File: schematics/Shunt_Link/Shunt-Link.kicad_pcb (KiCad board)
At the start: 2 copper layers, 78.2 x 96 mm, 33 parts, among them IC1 AD8221TRMZ-EP, IC2 AD8221TRMZ-EP, IC3 AD8221TRMZ-EP, IC4 AD8221TRMZ-EP, J1 PCIE-036-02-X-D-TH, J2 Conn_02x03_Odd_Even, J3 Conn_02x03_Odd_Even

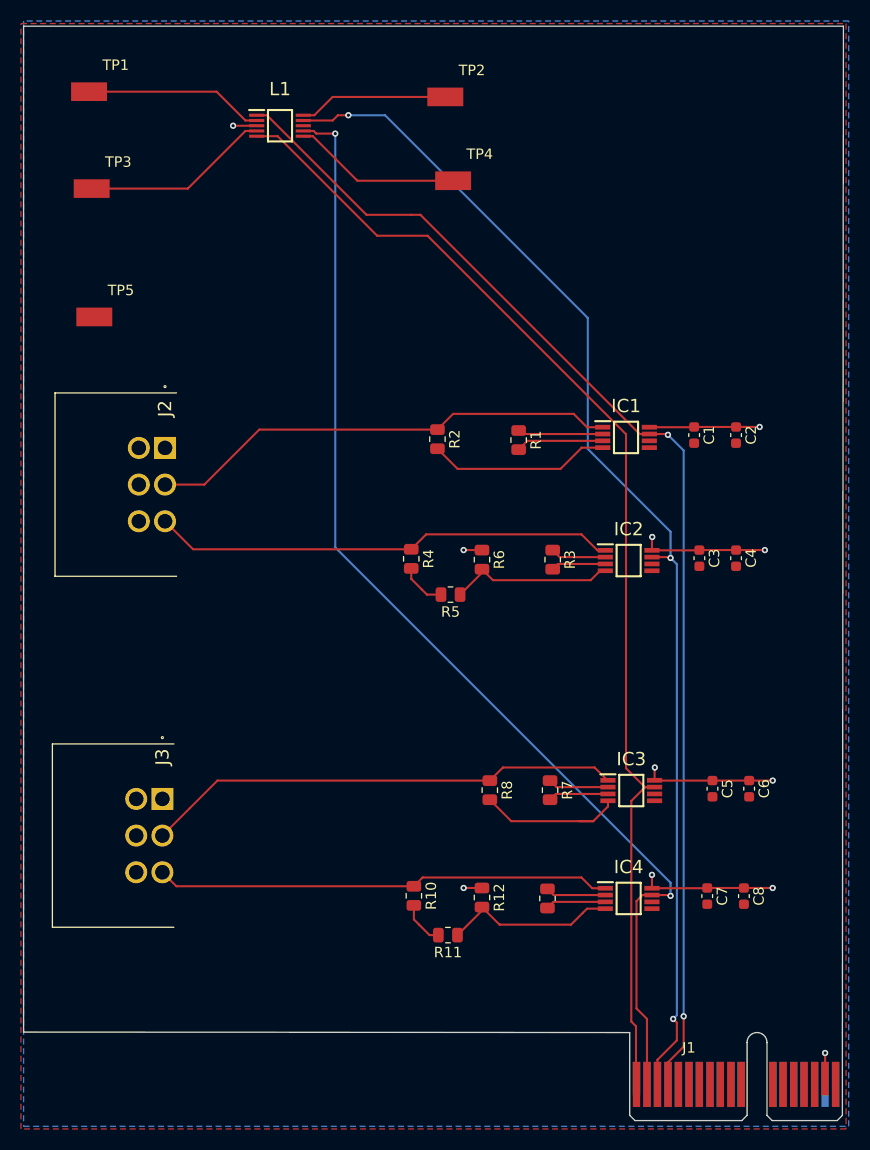
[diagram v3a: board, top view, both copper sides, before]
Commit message: Update libraries to one lib for all projects
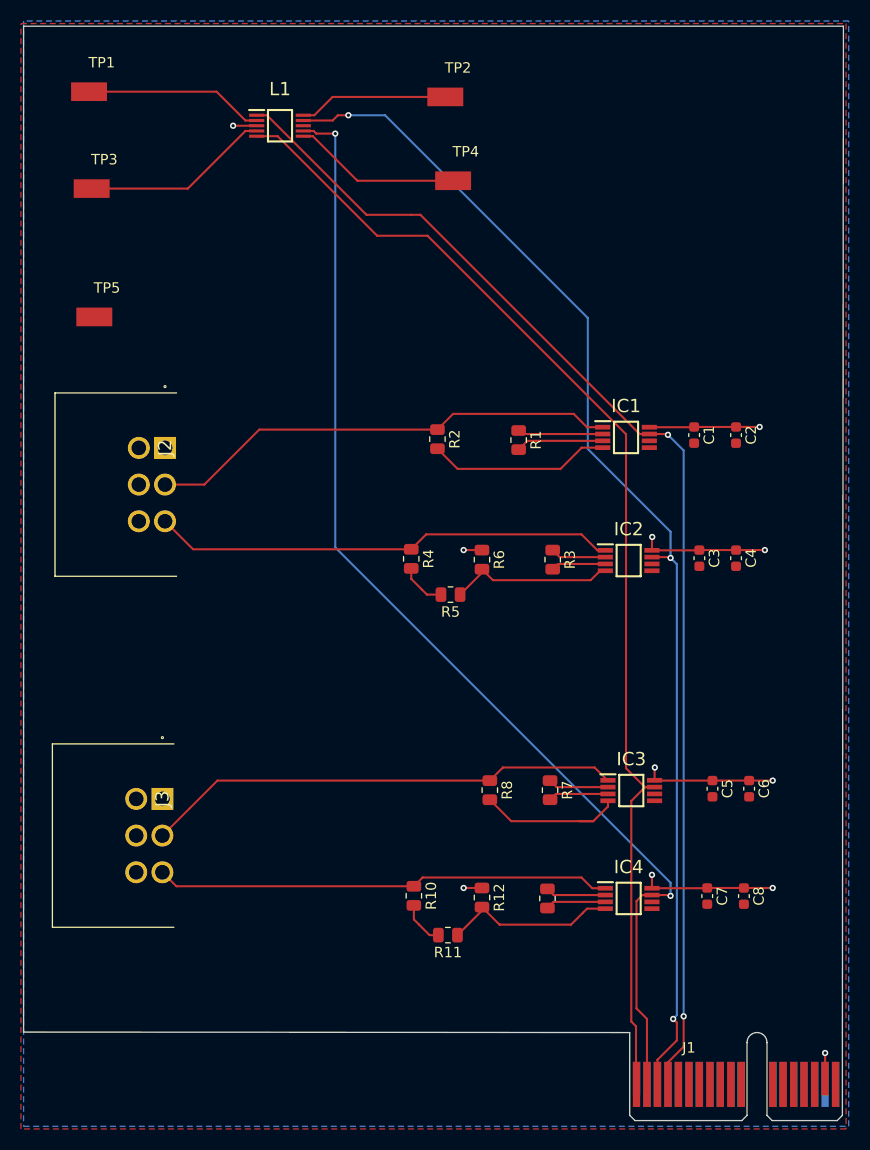
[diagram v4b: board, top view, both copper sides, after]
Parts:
- IC1, IC2, IC3, IC4: footprint Link_Footprints:AD8221TRMZ-EP -> Link Footprints:AD8221TRMZ
- J2, J3: footprint Link_Footprints:1818517 -> Link Footprints:PC-1818517
- L1: footprint Link_Footprints:AD8244ARMZ -> Link Footprints:AD8244ARMZ
- TP1, TP2, TP3, TP4, TP5: footprint Link_Footprints:KEYSTONE_5017 -> Link Footprints:Keystone_5017
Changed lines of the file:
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@@
 		)
 	)
-	(footprint "Link_Footprints:AD8221TRMZ-EP"
+	(footprint "Link Footprints:AD8221TRMZ"
 		(layer "F.Cu")
 		(at 135 66)
@@
 			)
 		)
+		(property "Field4" ""
+			(at 0 0 0)
+			(layer "F.SilkS")
+			(effects
+				(font
+					(size 1 1)
+					(thickness 0.1)
+				)
+			)
+		)
 		(property "Height" "1.1"
 			(at 0 0 0)
@@
 		)
 		(embedded_fonts no)
-		(model "C:/Users/smbea/OneDrive/Personal Files/School/Summer 2025/KiCad Lib Files/AD8221TRMZ/AD8221.step"
+		(model "${KIPRJMOD}/../libraries/models/AD8221TRMZ.step"
 			(offset
 				(xyz 0 0 0)
@@
 		(embedded_fonts no)
 	)
-	(footprint "Link_Footprints:KEYSTONE_5017"
+	(footprint "Link Footprints:Keystone_5017"
 		(layer "F.Cu")
 		(at 117.75 33.5)
 		(property "Reference" "TP2"
-			(at 2.54 -2.54 0)
+			(at 1.21 -2.775 0)
 			(layer "F.SilkS")
 			(effects
@@
 		)
 		(property "Value" "T1"
-			(at -2.54 -2.54 0)
+			(at 6.29 2.775 0)
 			(layer "F.Fab")
 			(effects
@@
 			(layer "F.Fab")
 		)
-		(pad "1" smd rect
+		(pad "TP" smd rect
 			(at 0 0)
 			(size 3.43 1.78)
 			(layers "F.Cu" "F.Mask" "F.Paste")
-			(net 52 "/T_{1test}")
-			(pinfunction "1")
-			(pintype "passive")
 			(solder_mask_margin 0.102)
 		)
 		(embedded_fonts no)
-		(model "C:/Users/smbea/OneDrive/Personal_Files/School/Fall_2025/OATS/avena-rs/schematics/KiCad Lib Files/Keystone_5017/5017.STEP"
+		(model "${KIPRJMOD}/../libraries/models/Keystone_5017.STEP"
 			(offset
 				(xyz 0 0 0)
@@
 		)
 	)
-	(footprint "Link_Footprints:AD8244ARMZ"
+	(footprint "Link Footprints:AD8244ARMZ"
 		(layer "F.Cu")
 		(at 101.975 36.25)
@@
 		)
 		(embedded_fonts no)
-		(model "C:/Users/smbea/OneDrive/Personal Files/School/Summer 2025/KiCad Lib Files/AD8244/AD8244ARMZ.stp"
+		(model "${KIPRJMOD}/../libraries/models/AD8244ARMZ.stp"
 			(offset
 				(xyz 0 0 0)
@@
 		)
 	)
-	(footprint "Link_Footprints:AD8221TRMZ-EP"
+	(footprint "Link Footprints:AD8221TRMZ"
 		(layer "F.Cu")
 		(at 135.5 99.7)
@@
 			)
 		)
+		(property "Field4" ""
+			(at 0 0 0)
+			(layer "F.SilkS")
+			(effects
+				(font
+					(size 1 1)
+					(thickness 0.1)
+				)
+			)
+		)
 		(property "Height" "1.1"
 			(at 0 0 0)
@@
 		)
 		(embedded_fonts no)
-		(model "C:/Users/smbea/OneDrive/Personal Files/School/Summer 2025/KiCad Lib Files/AD8221TRMZ/AD8221.step"
+		(model "${KIPRJMOD}/../libraries/models/AD8221TRMZ.step"
 			(offset
 				(xyz 0 0 0)
@@
 		)
 	)
-	(footprint "Link_Footprints:KEYSTONE_5017"
+	(footprint "Link Footprints:Keystone_5017"
 		(layer "F.Cu")
 		(at 83.75 33)
 		(property "Reference" "TP1"
-			(at 2.54 -2.54 0)
+			(at 1.21 -2.775 0)
 			(layer "F.SilkS")
 			(effects
@@
 		)
 		(property "Value" "S1"
-			(at -2.54 -2.54 0)
+			(at 6.29 2.775 0)
 			(layer "F.Fab")
 			(effects
@@
 			(layer "F.Fab")
 		)
-		(pad "1" smd rect
+		(pad "TP" smd rect
 			(at 0 0)
 			(size 3.43 1.78)
 			(layers "F.Cu" "F.Mask" "F.Paste")
-			(net 51 "/S_{1test}")
-			(pinfunction "1")
-			(pintype "passive")
 			(solder_mask_margin 0.102)
 		)
 		(embedded_fonts no)
-		(model "C:/Users/smbea/OneDrive/Personal_Files/School/Fall_2025/OATS/avena-rs/schematics/KiCad Lib Files/Keystone_5017/5017.STEP"
+		(model "${KIPRJMOD}/../libraries/models/Keystone_5017.STEP"
 			(offset
 				(xyz 0 0 0)
@@
 		)
 	)
-	(footprint "Link_Footprints:AD8221TRMZ-EP"
+	(footprint "Link Footprints:AD8221TRMZ"
 		(layer "F.Cu")
 		(at 135.25 77.75)
@@
 			)
 		)
+		(property "Field4" ""
+			(at 0 0 0)
+			(layer "F.SilkS")
+			(effects
+				(font
+					(size 1 1)
+					(thickness 0.1)
+				)
+			)
+		)
 		(property "Height" "1.1"
 			(at 0 0 0)
@@
 		)
 		(embedded_fonts no)
-		(model "C:/Users/smbea/OneDrive/Personal Files/School/Summer 2025/KiCad Lib Files/AD8221TRMZ/AD8221.step"
+		(model "${KIPRJMOD}/../libraries/models/AD8221TRMZ.step"
 			(offset
 				(xyz 0 0 0)
@@
 		)
 	)
-	(footprint "Link_Footprints:KEYSTONE_5017"
+	(footprint "Link Footprints:Keystone_5017"
 		(layer "F.Cu")
 		(at 84 42.25)
 		(property "Reference" "TP3"
-			(at 2.54 -2.54 0)
+			(at 1.21 -2.775 0)
 			(layer "F.SilkS")
 			(effects
@@
 		)
 		(property "Value" "S2"
-			(at -2.54 -2.54 0)
+			(at 6.29 2.775 0)
 			(layer "F.Fab")
 			(effects
@@
 			(layer "F.Fab")
 		)
-		(pad "1" smd rect
+		(pad "TP" smd rect
 			(at 0 0)
 			(size 3.43 1.78)
 			(layers "F.Cu" "F.Mask" "F.Paste")
-			(net 53 "/S_{2test}")
-			(pinfunction "1")
-			(pintype "passive")
 			(solder_mask_margin 0.102)
 		)
 		(embedded_fonts no)
-		(model "C:/Users/smbea/OneDrive/Personal_Files/School/Fall_2025/OATS/avena-rs/schematics/KiCad Lib Files/Keystone_5017/5017.STEP"
+		(model "${KIPRJMOD}/../libraries/models/Keystone_5017.STEP"
 			(offset
 				(xyz 0 0 0)
@@
 		)
 	)
-	(footprint "Link_Footprints:KEYSTONE_5017"
+	(footprint "Link Footprints:Keystone_5017"
 		(layer "F.Cu")
 		(at 84.25 54.5)
 		(property "Reference" "TP5"
-			(at 2.54 -2.54 0)
+			(at 1.21 -2.775 0)
 			(layer "F.SilkS")
 			(effects
@@
 		)
 		(property "Value" "GND"
-			(at -2.54 -2.54 0)
+			(at 6.29 2.775 0)
 			(layer "F.Fab")
 			(effects
@@
 			(layer "F.Fab")
 		)
-		(pad "1" smd rect
+		(pad "TP" smd rect
 			(at 0 0)
 			(size 3.43 1.78)
 			(layers "F.Cu" "F.Mask" "F.Paste")
-			(net 1 "GND")
-			(pinfunction "1")
-			(pintype "passive")
 			(solder_mask_margin 0.102)
 		)
 		(embedded_fonts no)
-		(model "C:/Users/smbea/OneDrive/Personal_Files/School/Fall_2025/OATS/avena-rs/schematics/KiCad Lib Files/Keystone_5017/5017.STEP"
+		(model "${KIPRJMOD}/../libraries/models/Keystone_5017.STEP"
 			(offset
 				(xyz 0 0 0)
@@
 		)
 	)
-	(footprint "Link_Footprints:KEYSTONE_5017"
+	(footprint "Link Footprints:Keystone_5017"
 		(layer "F.Cu")
 		(at 118.5 41.5)
 		(property "Reference" "TP4"
-			(at 2.54 -2.54 0)
+			(at 1.21 -2.775 0)
 			(layer "F.SilkS")
 			(effects
@@
 		)
 		(property "Value" "T2"
-			(at -2.54 -2.54 0)
+			(at 6.29 2.775 0)
 			(layer "F.Fab")
 			(effects
@@
 			(layer "F.Fab")
 		)
-		(pad "1" smd rect
+		(pad "TP" smd rect
 			(at 0 0)
 			(size 3.43 1.78)
 			(layers "F.Cu" "F.Mask" "F.Paste")
-			(net 50 "/T_{2test}")
-			(pinfunction "1")
-			(pintype "passive")
 			(solder_mask_margin 0.102)
 		)
 		(embedded_fonts no)
-		(model "C:/Users/smbea/OneDrive/Personal_Files/School/Fall_2025/OATS/avena-rs/schematics/KiCad Lib Files/Keystone_5017/5017.STEP"
+		(model "${KIPRJMOD}/../libraries/models/Keystone_5017.STEP"
 			(offset
 				(xyz 0 0 0)
@@
 		)
 	)
-	(footprint "Link_Footprints:1818517"
+	(footprint "Link Footprints:PC-1818517"
 		(layer "F.Cu")
 		(at 91 67 -90)
@@
 		(tags "Connector")
 		(property "Reference" "J2"
-			(at -3.75 0 90)
+			(at 0 0 90)
 			(layer "F.SilkS")
 			(effects
@@
 		)
 		(embedded_fonts no)
-		(model "C:/Users/smbea/OneDrive/Personal_Files/School/Fall_2025/OATS/avena-rs/schematics/KiCad Lib Files/PC-1818517/1818517.stp"
+		(model "${KIPRJMOD}/../libraries/models/PC-1818517.stp"
 			(offset
 				(xyz -5.459999956 -9.939999431 0)
@@
 		)
 	)
-	(footprint "Link_Footprints:AD8221TRMZ-EP"
+	(footprint "Link Footprints:AD8221TRMZ"
 		(layer "F.Cu")
 		(at 135.25 110)
@@
 			)
 		)
+		(property "Field4" ""
+			(at 0 0 0)
+			(layer "F.SilkS")
+			(effects
+				(font
+					(size 1 1)
+					(thickness 0.1)
+				)
+			)
+		)
 		(property "Height" "1.1"
 			(at 0 0 0)
@@
 		)
 		(embedded_fonts no)
-		(model "C:/Users/smbea/OneDrive/Personal Files/School/Summer 2025/KiCad Lib Files/AD8221TRMZ/AD8221.step"
+		(model "${KIPRJMOD}/../libraries/models/AD8221TRMZ.step"
 			(offset
 				(xyz 0 0 0)
@@
 		)
 	)
-	(footprint "Link_Footprints:1818517"
+	(footprint "Link Footprints:PC-1818517"
 		(layer "F.Cu")
 		(at 90.75 100.5 -90)
@@
 		(tags "Connector")
 		(property "Reference" "J3"
-			(at -4 0 90)
+			(at 0 0 270)
 			(layer "F.SilkS")
 			(effects
@@
 		)
 		(property "Value" "Conn_02x03_Odd_Even"
-			(at 0 0 90)
+			(at 0 0 270)
 			(layer "F.SilkS")
 			(hide yes)
@@
 		)
 		(property "Datasheet" ""
-			(at 0 0 90)
+			(at 0 0 270)
 			(layer "F.Fab")
 			(hide yes)
@@
 		)
 		(property "Description" "Generic connector, double row, 02x03, odd/even pin numbering scheme (row 1 odd numbers, row 2 even numbers), script generated (kicad-library-utils/schlib/autogen/connector/)"
-			(at 0 0 90)
+			(at 0 0 270)
 			(layer "F.Fab")
 			(hide yes)
@@
 		)
 		(fp_text user "${REFERENCE}"
-			(at 0 0 90)
+			(at 0 0 270)
 			(layer "F.Fab")
 			(effects
@@
 		)
 		(embedded_fonts no)
-		(model "C:/Users/smbea/OneDrive/Personal_Files/School/Fall_2025/OATS/avena-rs/schematics/KiCad Lib Files/PC-1818517/1818517.stp"
+		(model "${KIPRJMOD}/../libraries/models/PC-1818517.stp"
 			(offset
-				(xyz -5.25 -10.5 0)
+				(xyz -5.459999956 -9.939999431 0)
 			)
 			(scale
@@
 			)
 			(rotate
-				(xyz -0 -0 -0)
+				(xyz 0 0 0)
 			)
 		)
